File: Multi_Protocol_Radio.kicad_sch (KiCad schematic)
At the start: 6 parts, among them J2001 TC2050, J2002 Conn_01x06_Pin, J2003 Conn_01x06_Pin, U2001 MGM240PB32VNA3

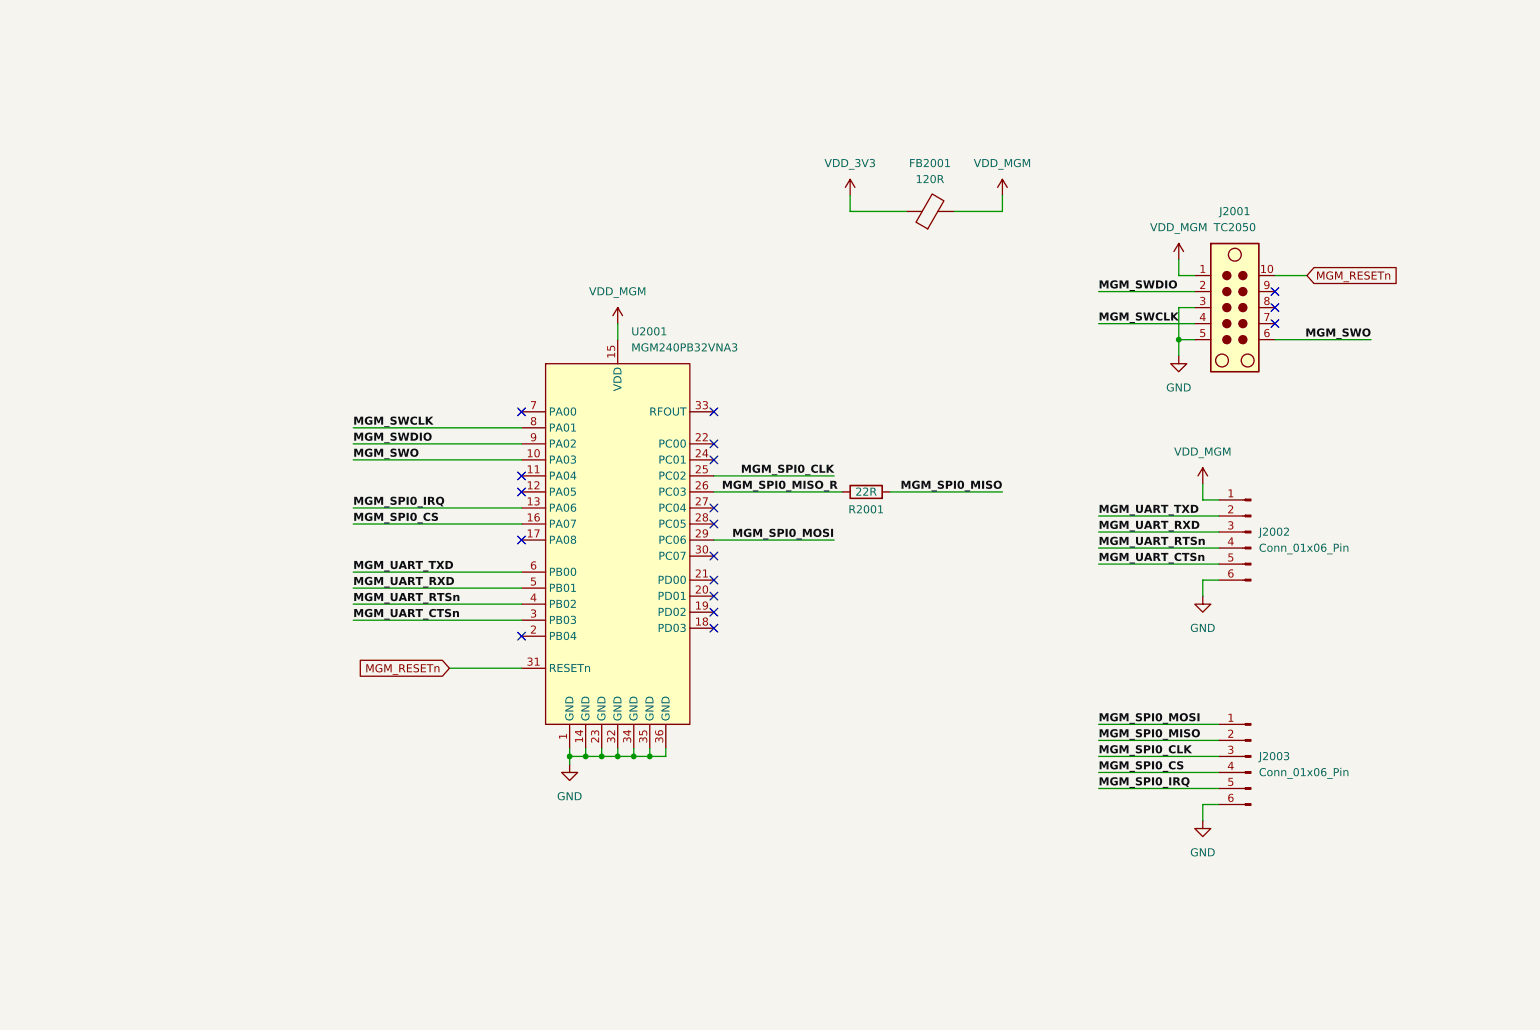
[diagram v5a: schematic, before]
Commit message: Added ground copper fill to L1 and L8
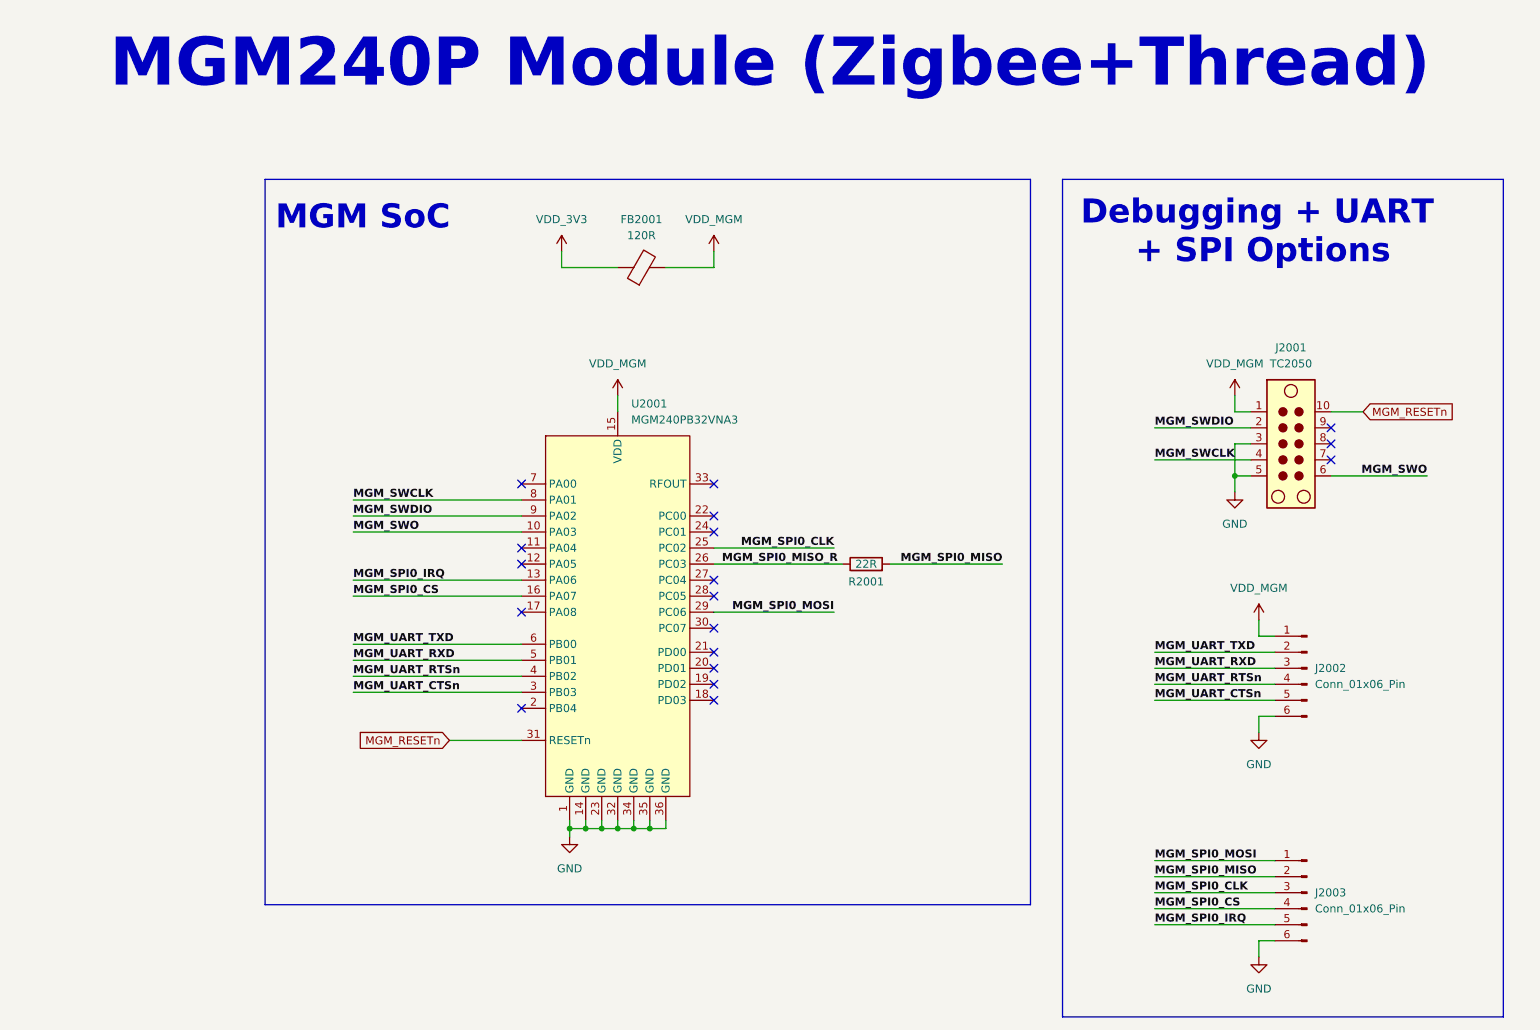
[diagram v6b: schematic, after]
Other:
- note added: "Debugging + UART + SPI Options"
- note added: "MGM SoC"
- note added: "MGM240P Module (Zigbee+Thread)"
- moved on the sheet: FB2001, J2001, J2002, J2003, R2001, U2001

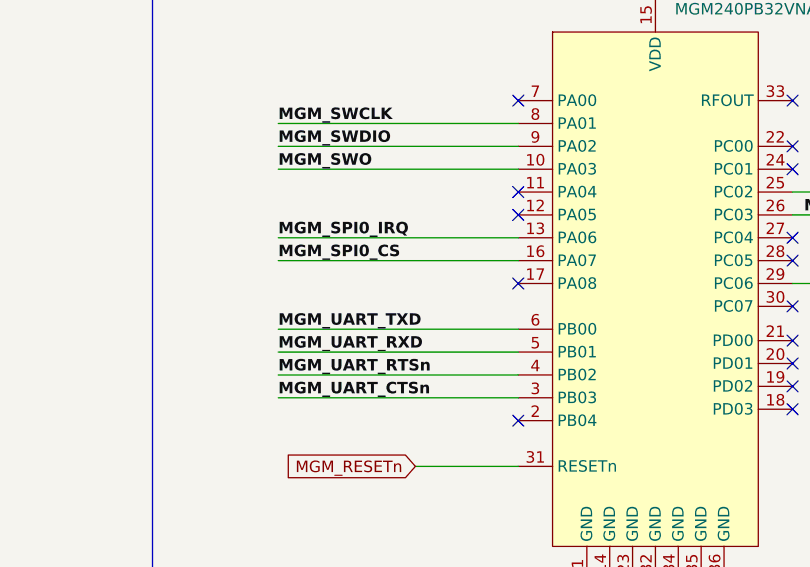
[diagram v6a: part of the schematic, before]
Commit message: Added status LEDs for SoC power, MGM240P power, and for GPIO0_70
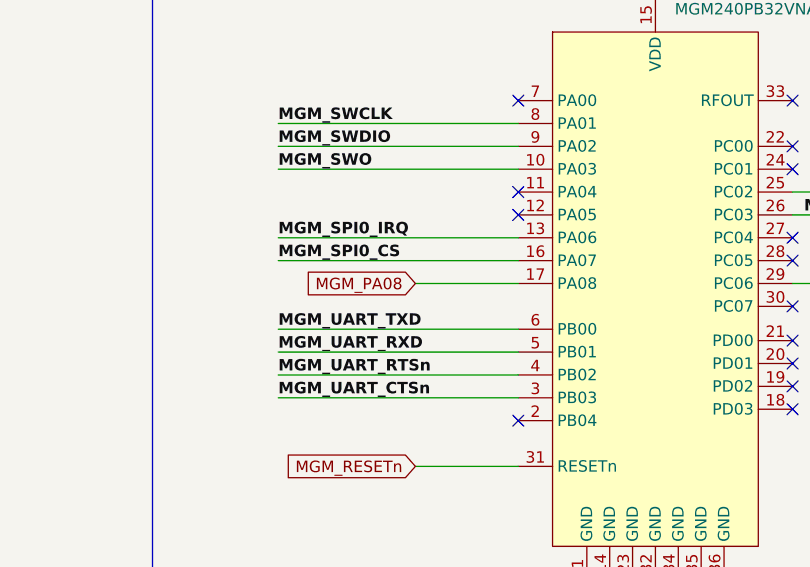
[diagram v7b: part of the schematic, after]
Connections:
- net MGM_PA08: now reaches U2001.17 (PA08)
- no-connect marks 18 -> 17
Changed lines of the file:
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@@
-	)
-	(no_connect
-		(at 90.17 114.3)
 	)
 	(no_connect
@@
 		(pts
 			(xy 107.95 148.59) (xy 107.95 147.32)
+		)
+		(stroke
+			(width 0)
+			(type default)
+		)
+	)
+	(wire
+		(pts
+			(xy 78.74 114.3) (xy 90.17 114.3)
 		)
 		(stroke
@@
 				(hide yes)
 			)
+		)
+	)
+	(global_label "MGM_PA08"
+		(shape input)
+		(at 78.74 114.3 180)
+		(fields_autoplaced yes)
+		(effects
+			(font
+				(size 1.27 1.27)
+			)
+			(justify right)
+		)
+		(property "Intersheetrefs" "${INTERSHEET_REFS}"
+			(at 65.8368 114.3 0)
+			(effects
+				(font
+					(size 1.27 1.27)
+				)
+				(justify right)
+				(hide yes)
+			)
